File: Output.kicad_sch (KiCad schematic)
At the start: 8 parts, among them U11 DM13a, U9 DM13a

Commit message: New schematic
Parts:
- removed U1: ~, mf:7seg_x8, symbol _mf:7seg_x8
- added U3: (no value), symbol _mf:7seg_x4
- added U4: (no value), mf:7seg_x8, symbol _mf:7seg_x8
- U2: value ~ -> (none)
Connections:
- net +5V: now also U2.1 (5V), U3.3 (5V), U4.1 (5V)
- net GND: now also U2.2 (GND), U3.4 (GND), U4.2 (GND)
- net LED_BC1: now reaches U9.14 (OUT9)
- net LED_BC2: now reaches U9.15 (OUT10)
- net LED_BC3: now reaches U9.16 (OUT11)
- net LED_BC4: now reaches U9.17 (OUT12)
- net LED_BC5: now reaches U9.18 (OUT13)
- net LED_BC6: now reaches U9.19 (OUT14)
- net LED_BC7: now reaches U9.20 (OUT15)
- net O_8_DIN: now reaches U2.3 (DIN)
- net O_8_CS: now reaches U2.4 (CS)
- new net: U2.8 (DOUT), U4.3 (DIN)
- new net: U2.9 (LODA), U4.4 (CS)
- new net: U2.10 (CLK), U4.5 (CLK)
- new net O_4_CLK: U3.1 (CLK)
- new net O_4_DIN: U3.2 (DIN)
- new net O_8_CLK: U2.5 (CLK)
- no-connect marks 0 -> 7

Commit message: Update schematic with nearly everything
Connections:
- net LED_BC1: now also U9.5 (OUT0); no longer U9.14 (OUT9)
- net LED_BC2: now also U9.6 (OUT1); no longer U9.15 (OUT10)
- net LED_BC3: now also U9.7 (OUT2); no longer U9.16 (OUT11)
- net LED_BC4: now also U9.8 (OUT3); no longer U9.17 (OUT12)
- net LED_BC5: now also U9.9 (OUT4); no longer U9.18 (OUT13)
- net LED_BC6: now also U9.10 (OUT5); no longer U9.19 (OUT14)
- net LED_BC7: now also U9.11 (OUT6); no longer U9.20 (OUT15)
- net LED_BC8: now reaches U9.12 (OUT7)
- net LED_BC9: now reaches U9.13 (OUT8)
- net LED_BC17: now reaches U11.5 (OUT0)
- net LED_BC18: now reaches U11.6 (OUT1)
- net LED_BC19: now reaches U11.7 (OUT2)
- net LED_BC20: now reaches U11.8 (OUT3)
- new net LED_BC10: U9.14 (OUT9)
- new net LED_BC11: U9.15 (OUT10)
- new net LED_BC12: U9.16 (OUT11)
- new net LED_BC13: U9.17 (OUT12)
- new net LED_BC14: U9.18 (OUT13)
- new net LED_BC15: U9.19 (OUT14)
- new net LED_BC16: U9.20 (OUT15)
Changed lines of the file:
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@@
+		)
+	)
+	(hierarchical_label "5V_LED"
+		(shape output)
+		(at 228.6 39.37 0)
+		(effects
+			(font
+				(size 1.27 1.27)
+			)
+			(justify left)
 		)
 	)
 	(hierarchical_label "LED_BC2"
 		(shape output)
+		(at 170.18 52.07 0)
+		(effects
+			(font
+				(size 1.27 1.27)
+			)
+			(justify left)
+		)
+	)
+	(hierarchical_label "LED_BC16"
+		(shape output)
+		(at 170.18 87.63 0)
+		(effects
+			(font
+				(size 1.27 1.27)
+			)
+			(justify left)
+		)
+	)
+	(hierarchical_label "LED_BC6"
+		(shape output)
+		(at 170.18 62.23 0)
+		(effects
+			(font
+				(size 1.27 1.27)
+			)
+			(justify left)
+		)
+	)
+	(hierarchical_label "LED_BC10"
+		(shape output)
+		(at 170.18 72.39 0)
+		(effects
+			(font
+				(size 1.27 1.27)
+			)
+			(justify left)
+		)
+	)
+	(hierarchical_label "LED_BC5"
+		(shape output)
+		(at 170.18 59.69 0)
+		(effects
+			(font
+				(size 1.27 1.27)
+			)
+			(justify left)
+		)
+	)
+	(hierarchical_label "LED_BC14"
+		(shape output)
+		(at 170.18 82.55 0)
+		(effects
+			(font
+				(size 1.27 1.27)
+			)
+			(justify left)
+		)
+	)
+	(hierarchical_label "LED_BC11"
+		(shape output)
 		(at 170.18 74.93 0)
 		(effects
@@
 		)
 	)
-	(hierarchical_label "LED_BC6"
+	(hierarchical_label "LED_BC12"
+		(shape output)
+		(at 170.18 77.47 0)
+		(effects
+			(font
+				(size 1.27 1.27)
+			)
+			(justify left)
+		)
+	)
+	(hierarchical_label "LED_BC18"
+		(shape output)
+		(at 241.3 52.07 0)
+		(effects
+			(font
+				(size 1.27 1.27)
+			)
+			(justify left)
+		)
+	)
+	(hierarchical_label "LED_BC7"
+		(shape output)
+		(at 170.18 64.77 0)
+		(effects
+			(font
+				(size 1.27 1.27)
+			)
+			(justify left)
+		)
+	)
+	(hierarchical_label "LED_BC1"
+		(shape output)
+		(at 170.18 49.53 0)
+		(effects
+			(font
+				(size 1.27 1.27)
+			)
+			(justify left)
+		)
+	)
+	(hierarchical_label "LED_BC8"
+		(shape output)
+		(at 170.18 67.31 0)
+		(effects
+			(font
+				(size 1.27 1.27)
+			)
+			(justify left)
+		)
+	)
+	(hierarchical_label "LED_BC4"
+		(shape output)
+		(at 170.18 57.15 0)
+		(effects
+			(font
+				(size 1.27 1.27)
+			)
+			(justify left)
+		)
+	)
+	(hierarchical_label "O_4_CLK"
+		(shape input)
+		(at 232.41 125.73 0)
+		(effects
+			(font
+				(size 1.27 1.27)
+			)
+			(justify left)
+		)
+	)
+	(hierarchical_label "O_DATA"
+		(shape input)
+		(at 264.16 109.22 0)
+		(effects
+			(font
+				(size 1.27 1.27)
+			)
+			(justify left)
+		)
+	)
+	(hierarchical_label "O_8_CLK"
+		(shape input)
+		(at 163.83 127 180)
+		(effects
+			(font
+				(size 1.27 1.27)
+			)
+			(justify right)
+		)
+	)
+	(hierarchical_label "O_4_DIN"
+		(shape input)
+		(at 232.41 123.19 0)
+		(effects
+			(font
+				(size 1.27 1.27)
+			)
+			(justify left)
+		)
+	)
+	(hierarchical_label "LED_BC3"
+		(shape output)
+		(at 170.18 54.61 0)
+		(effects
+			(font
+				(size 1.27 1.27)
+			)
+			(justify left)
+		)
+	)
+	(hierarchical_label "5V_LED"
+		(shape output)
+		(at 157.48 38.1 0)
+		(effects
+			(font
+				(size 1.27 1.27)
+			)
+			(justify left)
+		)
+	)
+	(hierarchical_label "LED_BC20"
+		(shape output)
+		(at 241.3 57.15 0)
+		(effects
+			(font
+				(size 1.27 1.27)
+			)
+			(justify left)
+		)
+	)
+	(hierarchical_label "O_8_CS"
+		(shape input)
+		(at 163.83 124.46 180)
+		(effects
+			(font
+				(size 1.27 1.27)
+			)
+			(justify right)
+		)
+	)
+	(hierarchical_label "O_CLK"
+		(shape input)
+		(at 264.16 104.14 0)
+		(effects
+			(font
+				(size 1.27 1.27)
+			)
+			(justify left)
+		)
+	)
+	(hierarchical_label "LED_BC17"
+		(shape output)
+		(at 241.3 49.53 0)
+		(effects
+			(font
+				(size 1.27 1.27)
+			)
+			(justify left)
+		)
+	)
+	(hierarchical_label "O_LATCH"
+		(shape input)
+		(at 264.16 106.68 0)
+		(effects
+			(font
+				(size 1.27 1.27)
+			)
+			(justify left)
+		)
+	)
+	(hierarchical_label "LED_BC9"
+		(shape output)
+		(at 170.18 69.85 0)
+		(effects
+			(font
+				(size 1.27 1.27)
+			)
+			(justify left)
+		)
+	)
+	(hierarchical_label "LED_BC19"
+		(shape output)
+		(at 241.3 54.61 0)
+		(effects
+			(font
+				(size 1.27 1.27)
+			)
+			(justify left)
+		)
+	)
+	(hierarchical_label "LED_BC13"
+		(shape output)
+		(at 170.18 80.01 0)
+		(effects
+			(font
+				(size 1.27 1.27)
+			)
+			(justify left)
+		)
+	)
+	(hierarchical_label "LED_BC15"
 		(shape output)
 		(at 170.18 85.09 0)
 		(effects
 			(font
-				(size 1.27 1.27)
-			)
-			(justify left)
-		)
-	)
-	(hierarchical_label "LED_BC5"
-		(shape output)
-		(at 170.18 82.55 0)
-		(effects
-			(font
-				(size 1.27 1.27)
-			)
-			(justify left)
-		)
-	)
-	(hierarchical_label "LED_BC7"
-		(shape output)
-		(at 170.18 87.63 0)
-		(effects
-			(font
-				(size 1.27 1.27)
-			)
-			(justify left)
-		)
-	)
-	(hierarchical_label "LED_BC1"
-		(shape output)
-		(at 170.18 72.39 0)
-		(effects
-			(font
-				(size 1.27 1.27)
-			)
-			(justify left)
-		)
-	)
-	(hierarchical_label "LED_BC4"
-		(shape output)
-		(at 170.18 80.01 0)
-		(effects
-			(font
-				(size 1.27 1.27)
-			)
-			(justify left)
-		)
-	)
-	(hierarchical_label "O_4_CLK"
-		(shape input)
-		(at 232.41 125.73 0)
-		(effects
-			(font
-				(size 1.27 1.27)
-			)
-			(justify left)
-		)
-	)
-	(hierarchical_label "O_DATA"
-		(shape input)
-		(at 264.16 109.22 0)
-		(effects
-			(font
-				(size 1.27 1.27)
-			)
-			(justify left)
-		)
-	)
-	(hierarchical_label "O_8_CLK"
-		(shape input)
-		(at 163.83 127 180)
-		(effects
-			(font
-				(size 1.27 1.27)
-			)
-			(justify right)
-		)
-	)
-	(hierarchical_label "O_4_DIN"
-		(shape input)
-		(at 232.41 123.19 0)
-		(effects
-			(font
-				(size 1.27 1.27)
-			)
-			(justify left)
-		)
-	)
-	(hierarchical_label "LED_BC3"
-		(shape output)
-		(at 170.18 77.47 0)
-		(effects
-			(font
-				(size 1.27 1.27)
-			)
-			(justify left)
-		)
-	)
-	(hierarchical_label "5V_LED"
-		(shape output)
-		(at 157.48 38.1 0)
-		(effects
-			(font
-				(size 1.27 1.27)
-			)
-			(justify left)
-		)
-	)
-	(hierarchical_label "O_8_CS"
-		(shape input)
-		(at 163.83 124.46 180)
-		(effects
-			(font
-				(size 1.27 1.27)
-			)
-			(justify right)
-		)
-	)
-	(hierarchical_label "O_CLK"
-		(shape input)
-		(at 264.16 104.14 0)
-		(effects
-			(font
-				(size 1.27 1.27)
-			)
-			(justify left)
-		)
-	)
-	(hierarchical_label "O_LATCH"
-		(shape input)
-		(at 264.16 106.68 0)
-		(effects
-			(font

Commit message: New pcb and 3 pos switch footprint
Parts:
- renumbered C6 to C10, C4 to C9
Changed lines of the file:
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@@
 		(dnp no)
 		(fields_autoplaced yes)
-		(property "Reference" "C6"
+		(property "Reference" "C10"
 			(at 199.39 43.18 0)
 			(hide yes)
@@
 			(project "mf"
 				(path "/12465328-c9f8-4b9f-925c-d562e2f7e62f/07bcd1df-bef5-4937-a043-adff33d82641"
-					(reference "C6")
+					(reference "C10")
 					(unit 1)
 				)
@@
 		(dnp no)
 		(fields_autoplaced yes)
-		(property "Reference" "C4"
+		(property "Reference" "C9"
 			(at 139.7 38.1 0)
 			(hide yes)
@@
 			(project "mf"
 				(path "/12465328-c9f8-4b9f-925c-d562e2f7e62f/07bcd1df-bef5-4937-a043-adff33d82641"
-					(reference "C4")
+					(reference "C9")
 					(unit 1)
 				)

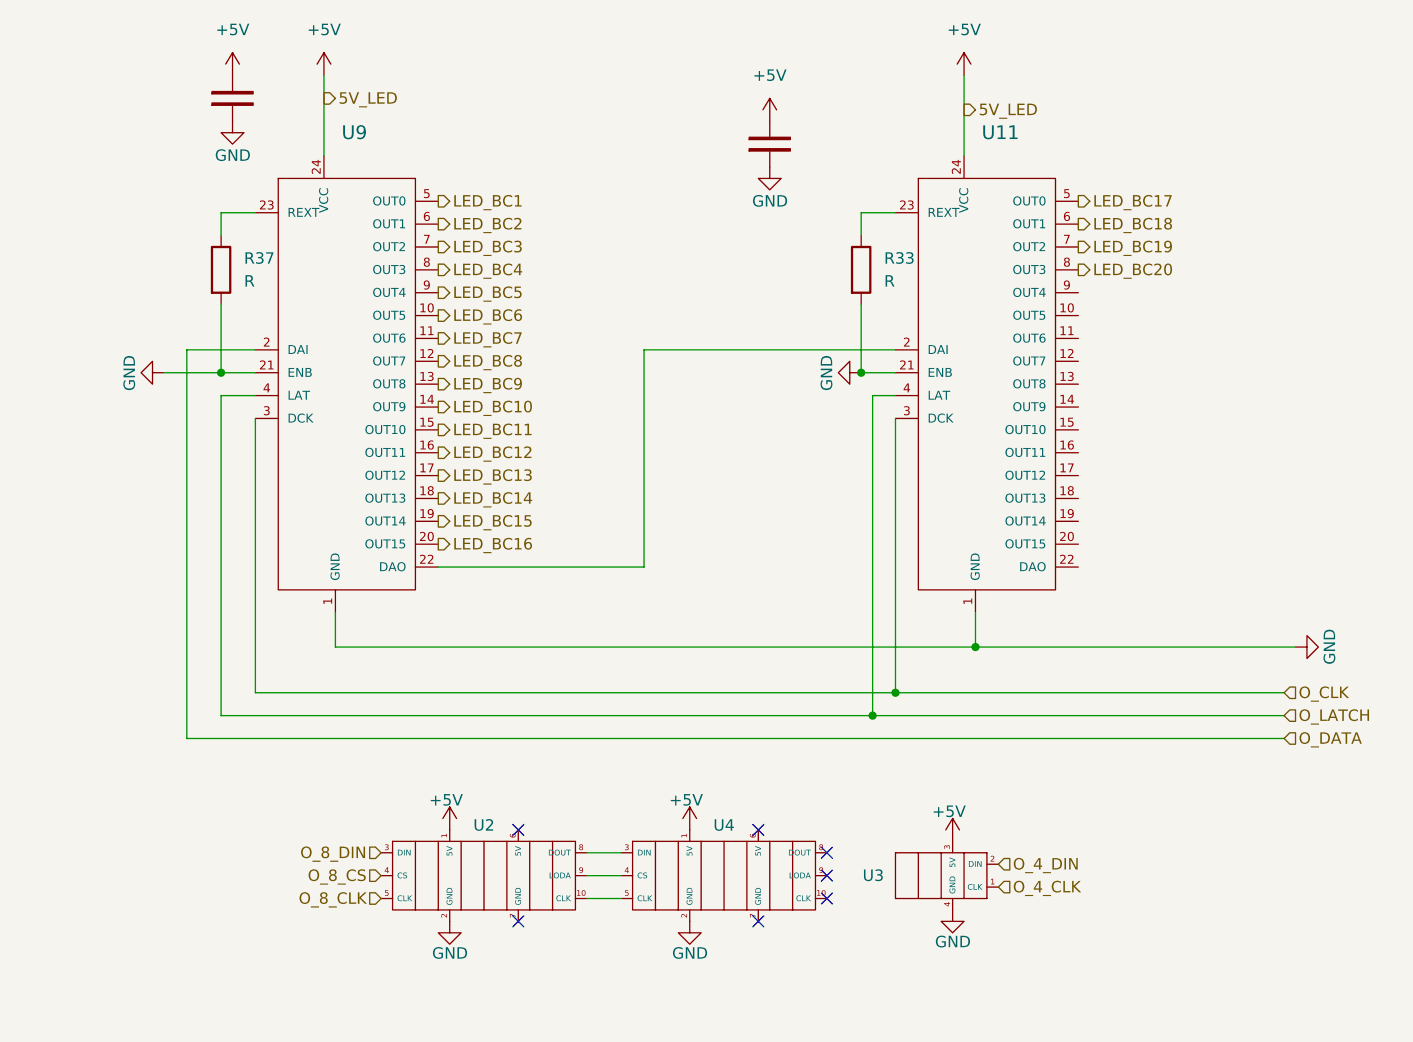
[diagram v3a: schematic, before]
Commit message: Begin PCB routing + change in schematic
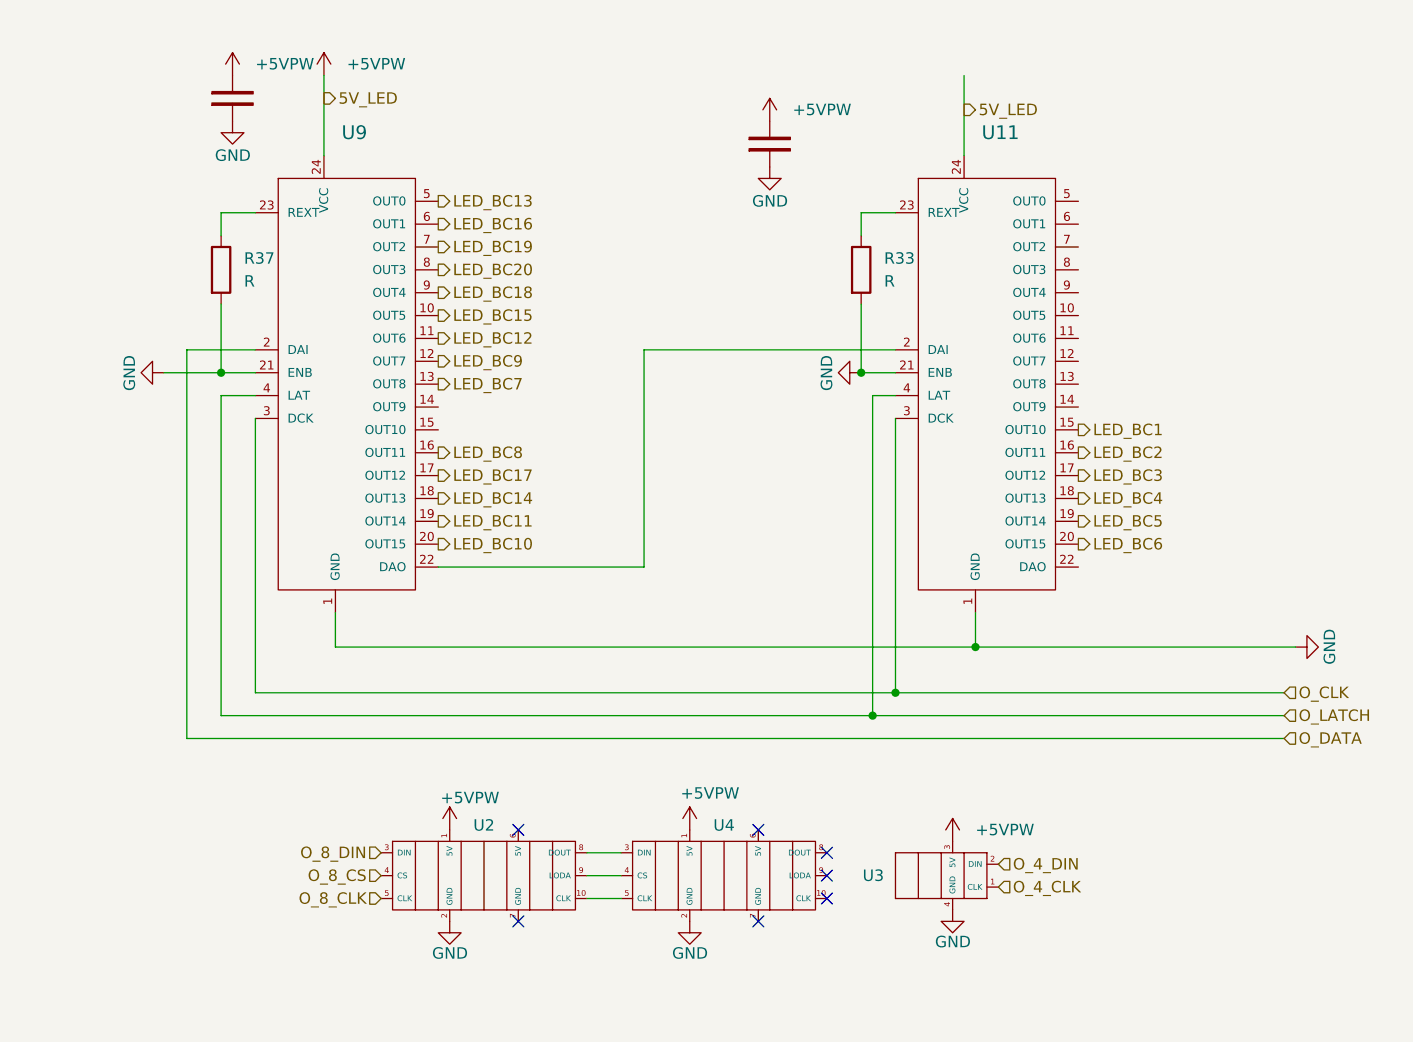
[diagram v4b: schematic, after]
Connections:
- net LED_BC1: now also U11.15 (OUT10); no longer U9.5 (OUT0)
- net LED_BC10: now also U9.20 (OUT15); no longer U9.14 (OUT9)
- net LED_BC11: now also U9.19 (OUT14); no longer U9.15 (OUT10)
- net LED_BC12: now also U9.11 (OUT6); no longer U9.16 (OUT11)
- net LED_BC13: now also U9.5 (OUT0); no longer U9.17 (OUT12)
- net LED_BC15: now also U9.10 (OUT5); no longer U9.19 (OUT14)
- net LED_BC16: now also U9.6 (OUT1); no longer U9.20 (OUT15)
- net LED_BC17: now also U9.17 (OUT12); no longer U11.5 (OUT0)
- net LED_BC18: now also U9.9 (OUT4); no longer U11.6 (OUT1)
- net LED_BC19: now also U9.7 (OUT2); no longer U11.7 (OUT2)
- net LED_BC2: now also U11.16 (OUT11); no longer U9.6 (OUT1)
- net LED_BC20: now also U9.8 (OUT3); no longer U11.8 (OUT3)
- net LED_BC3: now also U11.17 (OUT12); no longer U9.7 (OUT2)
- net LED_BC4: now also U11.18 (OUT13); no longer U9.8 (OUT3)
- net LED_BC5: now also U11.19 (OUT14); no longer U9.9 (OUT4)
- net LED_BC6: now also U11.20 (OUT15); no longer U9.10 (OUT5)
- net LED_BC7: now also U9.13 (OUT8); no longer U9.11 (OUT6)
- net LED_BC8: now also U9.16 (OUT11); no longer U9.12 (OUT7)
- net LED_BC9: now also U9.12 (OUT7); no longer U9.13 (OUT8)
- net +5V renamed +5VPW

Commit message: Nearly finished just need to add the footprint for the 5/6 pos switch and connect to the rest ! And it will be going into production !
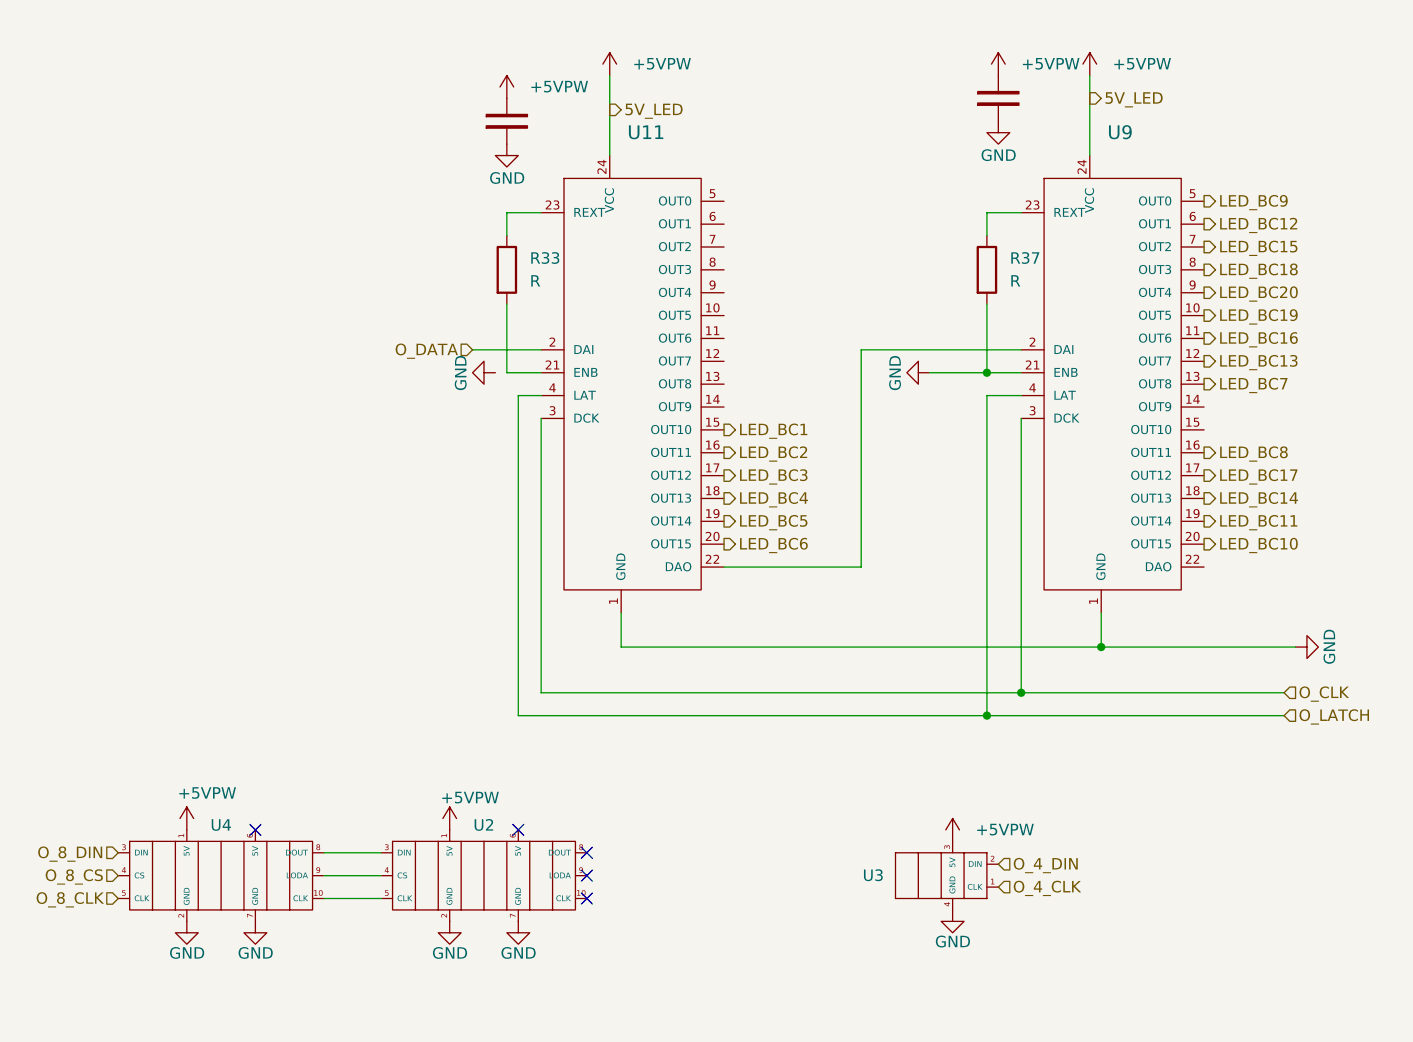
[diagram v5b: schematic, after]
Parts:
- U3: footprint (none) -> mf:7seg_x4
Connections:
- net GND: now also U2.7 (GND), U4.7 (GND); no longer R33.2, U11.21 (ENB)
- net LED_BC12: now also U9.6 (OUT1); no longer U9.11 (OUT6)
- net LED_BC13: now also U9.12 (OUT7); no longer U9.5 (OUT0)
- net LED_BC15: now also U9.7 (OUT2); no longer U9.10 (OUT5)
- net LED_BC16: now also U9.11 (OUT6); no longer U9.6 (OUT1)
- net LED_BC18: now also U9.8 (OUT3); no longer U9.9 (OUT4)
- net LED_BC19: now also U9.10 (OUT5); no longer U9.7 (OUT2)
- net LED_BC20: now also U9.9 (OUT4); no longer U9.8 (OUT3)
- net LED_BC9: now also U9.5 (OUT0); no longer U9.12 (OUT7)
- net O_8_CLK: now also U4.5 (CLK); no longer U2.5 (CLK)
- net O_8_CS: now also U4.4 (CS); no longer U2.4 (CS)
- net O_8_DIN: now also U4.3 (DIN); no longer U2.3 (DIN)
- net O_DATA: now also U11.2 (DAI); no longer U9.2 (DAI)
- net at U9.22 (DAO): no longer U11.2 (DAI)
- net at U4.10 (CLK): now also U2.5 (CLK)
- net at U2.8 (DOUT): no longer U4.3 (DIN)
- net at U2.9 (LODA): no longer U4.4 (CS)
- net at U2.10 (CLK): no longer U4.5 (CLK)
- net at U4.8 (DOUT): now also U2.3 (DIN)
- net at U4.9 (LODA): now also U2.4 (CS)
- net at U11.22 (DAO): now also U9.2 (DAI)
- new net: R33.2, U11.21 (ENB)
- no-connect marks 7 -> 5
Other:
- moved on the sheet: R33, R37, U11, U4, U9
